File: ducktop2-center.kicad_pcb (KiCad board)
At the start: 8 copper layers, 230 x 185 mm, 710 parts, among them J10 Amphenol MDT420M01001 M-key N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, J16 Case power/reset button harne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, J2300 FH12-30S 30-pin radio daughte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, J310 Mainboard keyboard FFC to MX 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, J4 TC2030 Cortex SWD: VTref/SWDI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, J40 Amphenol MDT420E01001 E-key W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, J41 SSD1306 OLED A 4-pin GND/VDD/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, J420 Left 8-ohm BTL speaker; pin 1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, J421 Right 8-ohm BTL speaker; pin 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, J422 CUI SJ1-3535NG rear 3.5mm ste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, J45 SSD1306 OLED B 4-pin GND/VDD/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, J52 Delta BFB04512HHA-CZ0T: GND, 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, J53 Lid/hall switch, J54 Skin/hinge NTC, J56 Mu heatsink/spreader NTC, J58 Field-soldered trackpad USB2 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, J73 Rear USB-C EC firmware progra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, J901 JST PUD 2x20 protected maker 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, J902 TC2030 Cortex SWD: VTref/SWDI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, Q13 CSD19537Q3 100V AUX reverse F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, Q14 BSS138 fast reverse-gate pull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, Q200 2N7002KT1G fan PWM open-drain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, Q21 SiSS4409DN 40V reverse-blocki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, Q22 SiSS4409DN 40V reverse-blocki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, Q23 SiSS4409DN 40V reverse-blocki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, Q2300 2N7002K radio-PG USB enable, Q24 SiSS4409DN 40V reverse-blocki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, Q25 CSD17575Q3 BQ25798 ship FET, Q60 2N7002 physical host-VBUS USB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, Q62 2N7002 DFU-mode USB mux force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, Q700 BSS138 active-high charger en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, Q702 BSS138 QON open-drain pulse, Q750 BSS138 fail-off EN/UVLO clamp, Q751 BSS138 active-high enable rel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, Q901 2N7002 physical host-VBUS USB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, Q903 2N7002 maker header isolation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, SW1 Reset, SW2 Mu Power, SW3 Mu Reset, SW4 BOOT0 (DFU), SW900 Maker reset/RUN, SW901 Maker BOOTSEL, U10 BQ34Z100-G1 protected-pack ga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, U12 TPS26630RGER 3A AUX eFuse / s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, U15 LTC4418IUF#PBF dual-input sel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, U170 SN74LVC3G34DCUR E-key control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, U2 BQ25798RQMR, U2300 TPS259470ARPW 2A reverse-bloc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, U2301 TLV803EA43 4.3V radio rail su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, U2302 SN74LVC1G17DBVR radio PG leve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, U2303 TS3USB30E default-disconnecte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, U2304 TPS2553D radio codec VBUS gat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, U2305 USBLC6-2P6 radio codec USB ESD, U310 TPS2553D keyboard RGB 5V swit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, U311 SN74AHCT1G126 keyboard RGB 3V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, U4 STM32F407VGTx, U400 USB2512B-AEZG-TR two-port HS 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, U401 TLV803EA29RDBZR 2.93V reset s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, U402 TPS2052BDR dual 500mA USB pow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, U410 PCM2900CDBR USB Audio Class s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, U420 TPA2012D2RTJR stereo BTL clas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, U421 SN74LVC1G08DBVR SSPND AND EC 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, U425 TPA6130A2RTJR DirectPath ster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, U430 LP5907MFX-2.8/NOPB low-noise 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, U431 TLV9061IDBVR microphone pream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, U44 TCA9539PWR resettable source 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, U45 TCA9548A service I2C mux @0x70, U46 SN74LVC1G08DBVR EC-reset-qual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, U5 TPS54202DDC, U6 TPS56637RPAR VSYS -> SYS_5V (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, U60 USBLC6-2P6 EC USB ESD, U61 TS3USB30EDGSR EC USB host-sta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, U62 TPD4E05U06 wired trackpad USB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, U63 USBLC6-2P6 EC DFU USB ESD, U64 TPS2553DDBVR trackpad 0.61A b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, U7 TPS56637RPAR VSYS -> SYS_3V3 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, U718 TPS259470ARPW aggregate EC AO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, U750 TPS552892RYQR 12V buck-boost, U769 SN74LVC1G08DBVR qualified hos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, U770 TPS2553DDBVR internal host VB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

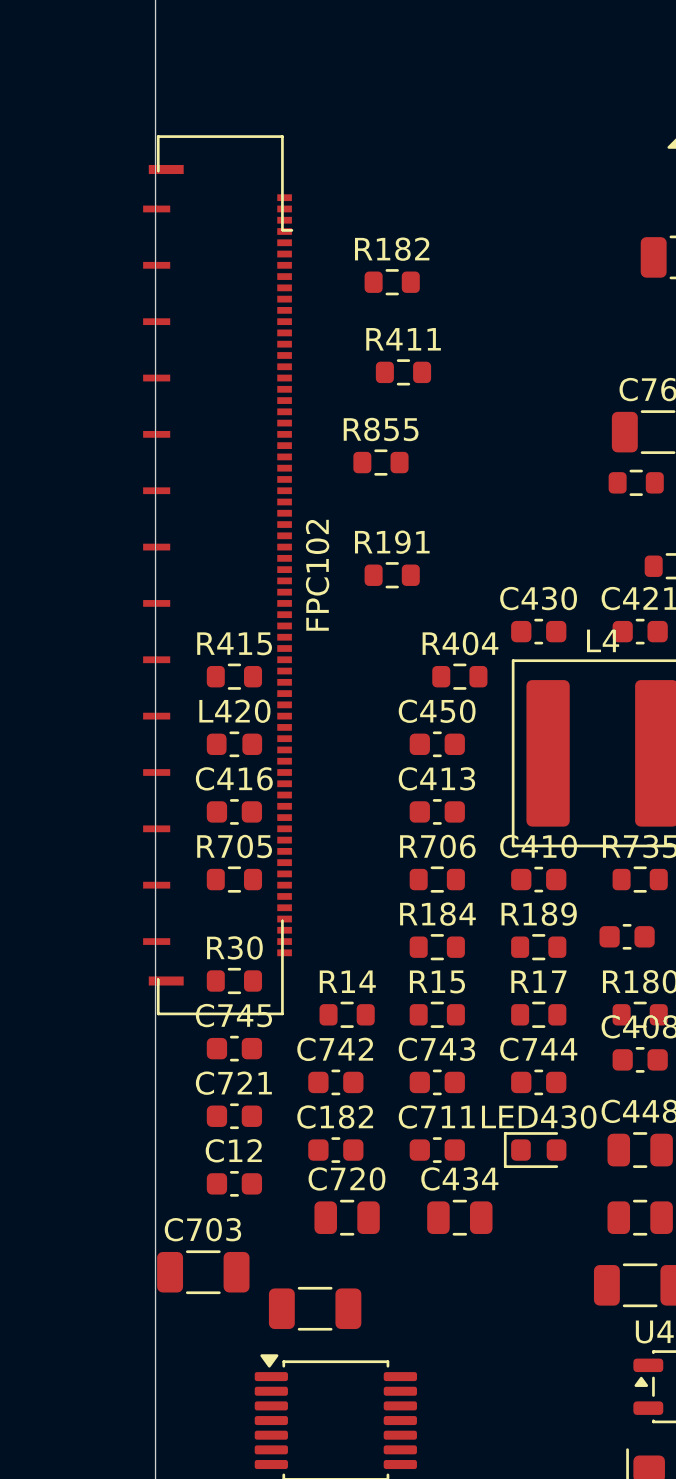
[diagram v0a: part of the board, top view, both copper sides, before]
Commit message: Deep audit completion: FPC anchors over cut lines, FPC106 rotation, pro rules
Follow-up fixes found while closing out the audit:
- FPC102/FPC104 FH41 MP tabs poked across the internal cut lines (pads
  physically off their boards): anchors moved to (73.5, 92.5) and
  (303.6, 92.5); all four boards now report 0 boundary crossings.
- FPC106 had reverted to the seam-away rotation; restored to (30, 54)
  rot 0 (cable enters from the BMS top edge).
- The MCP board sync clobbers the daughterboard .kicad_pro design rules;
  inherit_netclasses now restores them (min_through_hole 0.2, min_track
  0.09, min_clearance 0.09) so the DRC is honest about the 0.2mm drills.
- ERC triaged on all four projects: remaining items are cross-board
  power nets (driver on the other side of an FPC), power-flag artifacts,
  or intentional NCs -- no genuine errors.
- FH41-68S-0.5SH confirmed orderable (DigiKey/Mouser in stock).
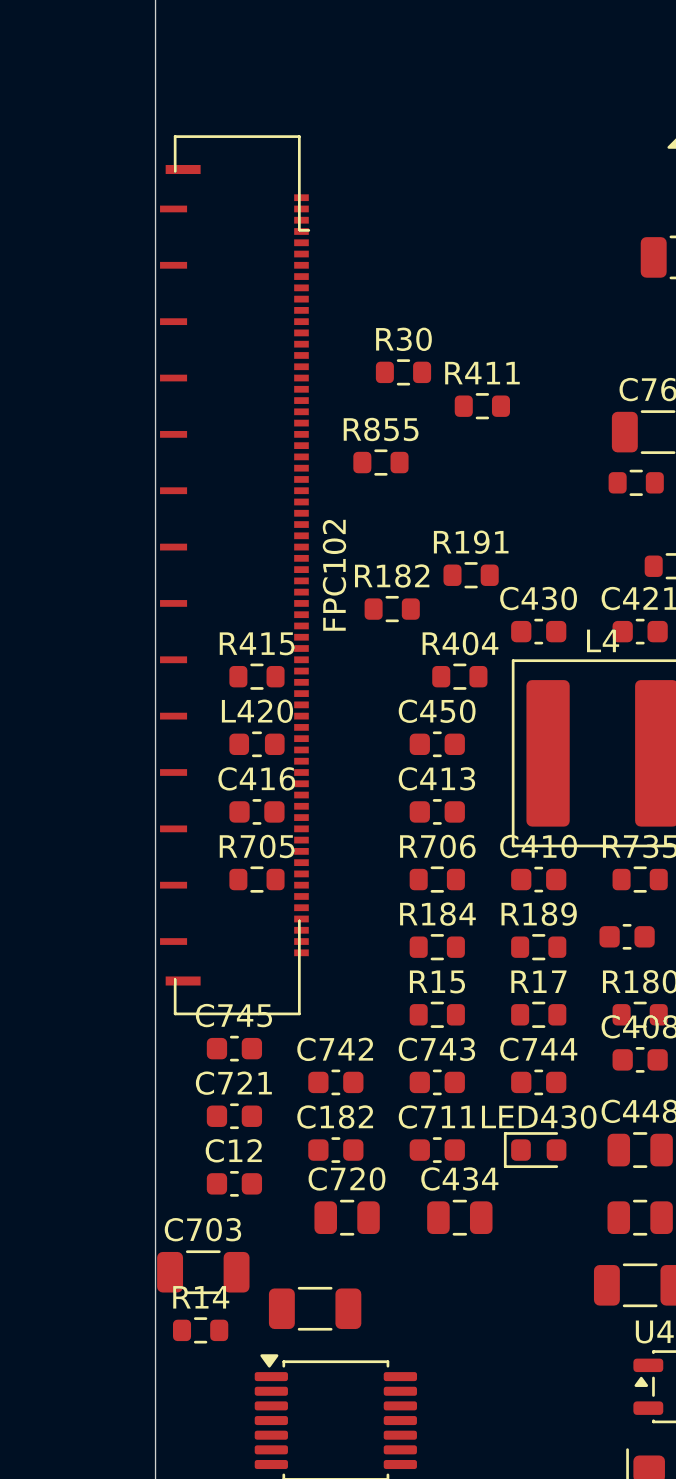
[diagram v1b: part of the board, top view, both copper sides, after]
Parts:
- moved R30 28.0 mm to (81.0, 83.5)
- moved R14 15.4 mm to (72.0, 126.0)
- moved R182 14.5 mm to (80.5, 94.0)
- moved R411 3.81 mm to (84.5, 85.0)
- moved R191 3.50 mm to (84.0, 92.5)
- moved C416 1.00 mm to (74.5, 103.0)
- moved L420 1.00 mm to (74.5, 100.0)
- moved R415 1.00 mm to (74.5, 97.0)
- moved R705 1.00 mm to (74.5, 106.0)
- moved FPC102 0.75 mm to (73.5, 92.5)

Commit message: Phase 5: second-opinion audit remediation + rebuilt, verified board pipeline
Second-opinion AI audit found A-tier defects; remediation applied and the
board pipeline rebuilt on a known-good base with the fixes it needed:

- electrical: LTC4418IUF symbol pinout corrected (both selectors were
  dead as drawn); center charge cascade (U15 <- U15B, PD1 > PD2 > AUX);
  pack negative never crosses FPC-3, 15-pin FG_VSS return; power-budgeted
  FPC pin maps (0.4 A/pin derate); J12/DS4 completed; AUX source fuse
- FH41-68S footprint: 13 datasheet-correct SH pads + SH pin in symbol
- connector geometry settled against the Hirose FH12 2D drawing: FFC
  enters opposite the solder pins (mouth = local +Y); reversed side-B
  maps are correct for the 180-deg-mounted pairs; rotations set so mouths
  face across every seam
- pipeline (generate_split_boards.py): per-pin pad-net resync from the
  netlists (kills shadow nets for good), netlist-exact name
  normalization, netlist-only part injection (cascade, probe headers),
  zone refill after outline swap, read-before-write race fixed, orphan
  parts dropped loudly, non-zero exit on unresolved overlaps
- monolith board relocated to old/monolith_ducktop2.kicad_pcb (placement
  oracle for the center cut only)

verified end state: 4 boards 0 shorts / 0 clearance / 0 drill, 0 boundary
crossings, 6/6 connectors contract-exact with mouths facing, 0 shadow
nets, gates PASS x4, ERC 0 x4. routing next (499 nets/board).
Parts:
- added C715: C_0402_1005Metric, C_0402_1005Metric, F.Cu at (141.0, 7.00)
- added C747: C_0603_1608Metric, C_0603_1608Metric, F.Cu at (141.0, 8.50)
- added C748: C_0603_1608Metric, C_0603_1608Metric, F.Cu at (141.0, 15.5)
- added C749: C_0603_1608Metric, C_0603_1608Metric, F.Cu at (141.0, 22.0)
- added J50: PinHeader_1x04_P2.54mm_Vertical, PinHeader_1x04_P2.54mm_Vertical, F.Cu at (141.0, 44.5)
- added J8: PinHeader_1x04_P2.54mm_Vertical, PinHeader_1x04_P2.54mm_Vertical, F.Cu at (186.0, 90.0)
- added Q26: Vishay_PowerPAK_1212-8_Single, Vishay_PowerPAK_1212-8_Single, F.Cu at (186.0, 102.0)
- added Q27: Vishay_PowerPAK_1212-8_Single, Vishay_PowerPAK_1212-8_Single, F.Cu at (186.0, 114.0)
- added Q28: Vishay_PowerPAK_1212-8_Single, Vishay_PowerPAK_1212-8_Single, F.Cu at (195.0, 30.0)
- added Q29: Vishay_PowerPAK_1212-8_Single, Vishay_PowerPAK_1212-8_Single, F.Cu at (195.0, 42.0)
- added R741: R_0603_1608Metric, R_0603_1608Metric, F.Cu at (195.0, 54.0)
- added R742: R_0603_1608Metric, R_0603_1608Metric, F.Cu at (195.0, 66.0)
- added R743: R_0603_1608Metric, R_0603_1608Metric, F.Cu at (195.0, 78.0)
- added R744: R_0603_1608Metric, R_0603_1608Metric, F.Cu at (150.0, 45.0)
- added R745: R_0603_1608Metric, R_0603_1608Metric, F.Cu at (150.0, 57.0)
- added R746: R_0603_1608Metric, R_0603_1608Metric, F.Cu at (150.0, 69.0)
- added R747: R_0603_1608Metric, R_0603_1608Metric, F.Cu at (159.0, 1.50)
- added U15B: ADI_UF20_QFN20_4x4_P0.5_EP2.45, ADI_UF20_QFN20_4x4_P0.5_EP2.45, F.Cu at (204.0, 42.0)
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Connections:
- net /EC & MCU/BOOT0_NET renamed /EC &amp; MCU/BOOT0_NET
- net /EC & MCU/BUCK_BOOT renamed /EC &amp; MCU/BUCK_BOOT
- net /EC & MCU/BUCK_FB renamed /EC &amp; MCU/BUCK_FB
- net /EC & MCU/BUCK_SW renamed /EC &amp; MCU/BUCK_SW
- net /EC & MCU/EC_SWD_VTREF renamed /EC &amp; MCU/EC_SWD_VTREF
- net /EC & MCU/HSE_IN renamed /EC &amp; MCU/HSE_IN
- net /EC & MCU/HSE_OUT renamed /EC &amp; MCU/HSE_OUT
- net /EC & MCU/HSE_XTAL_OUT renamed /EC &amp; MCU/HSE_XTAL_OUT
- net /EC & MCU/LSE_IN renamed /EC &amp; MCU/LSE_IN
- net /EC & MCU/LSE_OUT renamed /EC &amp; MCU/LSE_OUT
- net /EC & MCU/NRST_NET renamed /EC &amp; MCU/NRST_NET
- net /EC & MCU/SERVICE_MUX_RESET_REQ_N renamed /EC &amp; MCU/SERVICE_MUX_RESET_REQ_N
- net /EC & MCU/SOURCE_MGR_INT_N renamed /EC &amp; MCU/SOURCE_MGR_INT_N
- net /EC & MCU/SWCLK_NET renamed /EC &amp; MCU/SWCLK_NET
- net /EC & MCU/SWDIO_NET renamed /EC &amp; MCU/SWDIO_NET
- net /EC & MCU/VCAP1_NODE renamed /EC &amp; MCU/VCAP1_NODE
- net /EC & MCU/VCAP2_NODE renamed /EC &amp; MCU/VCAP2_NODE
- net /Power & Battery/AON_EFUSE_DVDT renamed /Power &amp; Battery/AON_EFUSE_DVDT
- net /Power & Battery/AON_EFUSE_ILM renamed /Power &amp; Battery/AON_EFUSE_ILM
- net /Power & Battery/AON_EFUSE_OV renamed /Power &amp; Battery/AON_EFUSE_OV
- net /Power & Battery/AON_EFUSE_UV renamed /Power &amp; Battery/AON_EFUSE_UV
- net /Power & Battery/AON_OR_RAW renamed /Power &amp; Battery/AON_OR_RAW
- net /Power & Battery/AUX_DC_DIV renamed /Power &amp; Battery/AUX_DC_DIV
- net /Power & Battery/AUX_DC_FUSED renamed /Power &amp; Battery/AUX_DC_FUSED
- net /Power & Battery/AUX_EFUSE_BGATE renamed /Power &amp; Battery/AUX_EFUSE_BGATE
- net /Power & Battery/AUX_EFUSE_DRV renamed /Power &amp; Battery/AUX_EFUSE_DRV
- net /Power & Battery/AUX_EFUSE_DVDT renamed /Power &amp; Battery/AUX_EFUSE_DVDT
- net /Power & Battery/AUX_EFUSE_ILIM renamed /Power &amp; Battery/AUX_EFUSE_ILIM
- net /Power & Battery/AUX_EFUSE_IN_SYS renamed /Power &amp; Battery/AUX_EFUSE_IN_SYS
- net /Power & Battery/AUX_EFUSE_OV renamed /Power &amp; Battery/AUX_EFUSE_OV
- net /Power & Battery/AUX_EFUSE_Q2_GATE renamed /Power &amp; Battery/AUX_EFUSE_Q2_GATE
- net /Power & Battery/AUX_EFUSE_UV renamed /Power &amp; Battery/AUX_EFUSE_UV
- net /Power & Battery/AUX_PGTH renamed /Power &amp; Battery/AUX_PGTH
- net /Power & Battery/BATP_SENSE renamed /Power &amp; Battery/BATP_SENSE
- net /Power & Battery/BAT_CHARGER renamed /Power &amp; Battery/BAT_CHARGER
- net /Power & Battery/BTST1_NODE renamed /Power &amp; Battery/BTST1_NODE
- net /Power & Battery/BTST2_NODE renamed /Power &amp; Battery/BTST2_NODE
- net /Power & Battery/CHG_CE_HW_N renamed /Power &amp; Battery/CHG_CE_HW_N
- net /Power & Battery/CHG_TS_FIXED renamed /Power &amp; Battery/CHG_TS_FIXED
- net /Power & Battery/FG_BAT_DIV renamed /Power &amp; Battery/FG_BAT_DIV
- net /Power & Battery/FG_BAT_SENSE renamed /Power &amp; Battery/FG_BAT_SENSE
- net /Power & Battery/FG_CE renamed /Power &amp; Battery/FG_CE
- net /Power & Battery/FG_P1_TIE renamed /Power &amp; Battery/FG_P1_TIE
- net /Power & Battery/FG_REG25 renamed /Power &amp; Battery/FG_REG25
- net /Power & Battery/FG_SRN renamed /Power &amp; Battery/FG_SRN
- net /Power & Battery/FG_SRP renamed /Power &amp; Battery/FG_SRP
- net /Power & Battery/FG_TS renamed /Power &amp; Battery/FG_TS
- net /Power & Battery/ILIM_SET renamed /Power &amp; Battery/ILIM_SET
- net /Power & Battery/MAIN_SEL_TMR renamed /Power &amp; Battery/MAIN_SEL_TMR
- net /Power & Battery/PMIC_QON_PIN renamed /Power &amp; Battery/PMIC_QON_PIN
- net /Power & Battery/PMID renamed /Power &amp; Battery/PMID
- net /Power & Battery/PROG_SET renamed /Power &amp; Battery/PROG_SET
- net /Power & Battery/REGN renamed /Power &amp; Battery/REGN
- net /Power & Battery/SDRV_GATE renamed /Power &amp; Battery/SDRV_GATE
- net /Power & Battery/STAT_DRV renamed /Power &amp; Battery/STAT_DRV
- net /Power & Battery/STAT_LED_A renamed /Power &amp; Battery/STAT_LED_A
- net /Power & Battery/SW1 renamed /Power &amp; Battery/SW1
- net /Power & Battery/SW2 renamed /Power &amp; Battery/SW2
- net /Power & Battery/USB_MAIN_FET_COMMON renamed /Power &amp; Battery/USB_MAIN_FET_COMMON
- net /Power & Battery/USB_MAIN_GATE renamed /Power &amp; Battery/USB_MAIN_GATE
- net /Power & Battery/USB_MAIN_OV renamed /Power &amp; Battery/USB_MAIN_OV
- net /Power & Battery/USB_MAIN_UV renamed /Power &amp; Battery/USB_MAIN_UV
- net /Power & Battery/VBUS_DAMP renamed /Power &amp; Battery/VBUS_DAMP
- net /Wi-Fi/Bluetooth & OLEDs/OLED_A_SCL renamed /Wi-Fi/Bluetooth &amp; OLEDs/OLED_A_SCL
- net /Wi-Fi/Bluetooth & OLEDs/OLED_A_SDA renamed /Wi-Fi/Bluetooth &amp; OLEDs/OLED_A_SDA
- net /Wi-Fi/Bluetooth & OLEDs/OLED_B_SCL renamed /Wi-Fi/Bluetooth &amp; OLEDs/OLED_B_SCL
- net /Wi-Fi/Bluetooth & OLEDs/OLED_B_SDA renamed /Wi-Fi/Bluetooth &amp; OLEDs/OLED_B_SDA
- net /Wi-Fi/Bluetooth & OLEDs/WIFI_3V3 renamed /Wi-Fi/Bluetooth &amp; OLEDs/WIFI_3V3
- net /Wi-Fi/Bluetooth & OLEDs/WIFI_PERST_N renamed /Wi-Fi/Bluetooth &amp; OLEDs/WIFI_PERST_N
- net /Wi-Fi/Bluetooth & OLEDs/WIFI_REFCLK_E_N renamed /Wi-Fi/Bluetooth &amp; OLEDs/WIFI_REFCLK_E_N
- net /Wi-Fi/Bluetooth & OLEDs/WIFI_REFCLK_E_P renamed /Wi-Fi/Bluetooth &amp; OLEDs/WIFI_REFCLK_E_P
- net /Wi-Fi/Bluetooth & OLEDs/WIFI_W_DISABLE1_N renamed /Wi-Fi/Bluetooth &amp; OLEDs/WIFI_W_DISABLE1_N
- net /Wi-Fi/Bluetooth & OLEDs/WIFI_W_DISABLE2_N renamed /Wi-Fi/Bluetooth &amp; OLEDs/WIFI_W_DISABLE2_N
- A1 pad 104: (no net) -> unconnected-(A1-~{SMB_ALERT}-Pad104)
- A1 pad 106: (no net) -> unconnected-(A1-SMB_CLK-Pad106)
- A1 pad 108: (no net) -> unconnected-(A1-SMB_DATA-Pad108)
- A1 pad 112: (no net) -> unconnected-(A1-USB2_P6+-Pad112)
- A1 pad 114: (no net) -> unconnected-(A1-USB2_P6--Pad114)
- A1 pad 117: (no net) -> unconnected-(A1-~{PROCHOT}-Pad117)
- A1 pad 118: (no net) -> unconnected-(A1-GPP_F16-Pad118)
- A1 pad 119: (no net) -> unconnected-(A1-GPP_E0-Pad119)
- A1 pad 120: (no net) -> unconnected-(A1-GPP_F15-Pad120)
- A1 pad 121: (no net) -> unconnected-(A1-GPP_A12-Pad121)
- A1 pad 122: (no net) -> unconnected-(A1-GPP_F14-Pad122)
- A1 pad 123: (no net) -> unconnected-(A1-GPP_B14-Pad123)
- A1 pad 124: (no net) -> unconnected-(A1-GPP_F13-Pad124)
- A1 pad 125: (no net) -> unconnected-(A1-GPP_B11-Pad125)
- A1 pad 126: (no net) -> unconnected-(A1-GPP_F12-Pad126)
- A1 pad 127: (no net) -> unconnected-(A1-TPM_IRQ-Pad127)
- A1 pad 128: (no net) -> unconnected-(A1-GPP_D0-Pad128)
- A1 pad 130: (no net) -> unconnected-(A1-GPP_D1-Pad130)
- A1 pad 131: (no net) -> unconnected-(A1-SUSCLK-Pad131)
- A1 pad 132: (no net) -> unconnected-(A1-GPP_D2-Pad132)
- A1 pad 133: (no net) -> unconnected-(A1-~{BIOS_SEL}-Pad133)
- A1 pad 134: (no net) -> unconnected-(A1-GPP_D3-Pad134)
- A1 pad 137: (no net) -> unconnected-(A1-UART0_RXD-Pad137)
- A1 pad 138: (no net) -> unconnected-(A1-UART2_TXD-Pad138)
- A1 pad 139: (no net) -> unconnected-(A1-UART0_TXD-Pad139)
- A1 pad 140: (no net) -> unconnected-(A1-UART2_RXD-Pad140)
- A1 pad 141: (no net) -> unconnected-(A1-UART1_RXD-Pad141)
- A1 pad 142: (no net) -> unconnected-(A1-I2C5_SCL-Pad142)
- A1 pad 143: (no net) -> unconnected-(A1-UART1_TXD-Pad143)
- A1 pad 144: (no net) -> unconnected-(A1-I2C5_SDA-Pad144)
- A1 pad 145: (no net) -> unconnected-(A1-SML1_DATA-Pad145)
- A1 pad 146: (no net) -> unconnected-(A1-I2C4_SCL-Pad146)
- A1 pad 147: (no net) -> unconnected-(A1-SML1_CLK-Pad147)
- A1 pad 148: (no net) -> unconnected-(A1-I2C4_SDA-Pad148)
- A1 pad 149: (no net) -> unconnected-(A1-~{SML1_ALERT}-Pad149)
- A1 pad 150: (no net) -> unconnected-(A1-I2C3_SCL-Pad150)
- A1 pad 152: (no net) -> unconnected-(A1-I2C3_SDA-Pad152)
- A1 pad 153: (no net) -> unconnected-(A1-SPI_IO3-Pad153)
- A1 pad 154: (no net) -> unconnected-(A1-I2C2_SCL-Pad154)
- A1 pad 155: (no net) -> unconnected-(A1-SPI_CLK-Pad155)
- A1 pad 156: (no net) -> unconnected-(A1-I2C2_SDA-Pad156)
- A1 pad 157: (no net) -> unconnected-(A1-~{SPI_CS2}-Pad157)
- A1 pad 159: (no net) -> unconnected-(A1-SPI_MOSI/SPI_IO0-Pad159)
- A1 pad 160: (no net) -> unconnected-(A1-I2S_MCLK-Pad160)
- A1 pad 161: (no net) -> unconnected-(A1-SPI_IO2-Pad161)
- A1 pad 162: (no net) -> unconnected-(A1-I2S_SCLK-Pad162)
- A1 pad 163: (no net) -> unconnected-(A1-SPI_MISO/SPI_IO1-Pad163)
- A1 pad 164: (no net) -> unconnected-(A1-I2S_SFRM-Pad164)
- A1 pad 165: (no net) -> unconnected-(A1-~{SPI_CS}-Pad165)
- A1 pad 166: (no net) -> unconnected-(A1-I2S_TXD-Pad166)
- A1 pad 168: (no net) -> unconnected-(A1-I2S_RXD-Pad168)
- A1 pad 169: (no net) -> unconnected-(A1-DDIB_DDC_SDA-Pad169)
- A1 pad 171: (no net) -> unconnected-(A1-DDIB_DDC_SCL-Pad171)
- A1 pad 172: (no net) -> unconnected-(A1-HDA_RST-Pad172)
- A1 pad 173: (no net) -> unconnected-(A1-TCP1_DDC_SDA-Pad173)
- A1 pad 174: (no net) -> unconnected-(A1-HDA_BCLK-Pad174)
- A1 pad 175: (no net) -> unconnected-(A1-TCP1_DDC_SCL-Pad175)
- A1 pad 176: (no net) -> unconnected-(A1-HDA_SYNC-Pad176)
- A1 pad 178: (no net) -> unconnected-(A1-HDA_SDOUT-Pad178)
- A1 pad 180: (no net) -> unconnected-(A1-HDA_SDIN-Pad180)
- A1 pad 183: (no net) -> unconnected-(A1-DDIB_HPD-Pad183)
- A1 pad 184: (no net) -> unconnected-(A1-CSI_D_CK+-Pad184)
- A1 pad 185: (no net) -> unconnected-(A1-TCP1_HPD-Pad185)
- A1 pad 186: (no net) -> unconnected-(A1-CSI_D_CK--Pad186)
- A1 pad 190: (no net) -> unconnected-(A1-CSI_D_D1+/CSI_C_D2+-Pad190)
- A1 pad 191: (no net) -> unconnected-(A1-DDIB_AUX--Pad191)
- A1 pad 192: (no net) -> unconnected-(A1-CSI_D_D1-/CSI_C_D2--Pad192)
- A1 pad 193: (no net) -> unconnected-(A1-DDIB_AUX+-Pad193)
- A1 pad 196: (no net) -> unconnected-(A1-CSI_D_D0+/CSI_C_D3+-Pad196)
- A1 pad 197: (no net) -> unconnected-(A1-DDIB_TX3--Pad197)
- A1 pad 198: (no net) -> unconnected-(A1-CSI_D_D0-/CSI_C_D3--Pad198)
- A1 pad 199: (no net) -> unconnected-(A1-DDIB_TX3+-Pad199)
- A1 pad 2: (no net) -> unconnected-(A1-FAN1_PWM-Pad2)
- A1 pad 202: (no net) -> unconnected-(A1-CSI_C_CK+-Pad202)
- A1 pad 203: (no net) -> unconnected-(A1-DDIB_TX2--Pad203)
- A1 pad 204: (no net) -> unconnected-(A1-CSI_C_CK--Pad204)
- A1 pad 205: (no net) -> unconnected-(A1-DDIB_TX2+-Pad205)
- A1 pad 208: (no net) -> unconnected-(A1-CSI_C_D1+-Pad208)
- A1 pad 209: (no net) -> unconnected-(A1-DDIB_TX1--Pad209)
- A1 pad 210: (no net) -> unconnected-(A1-CSI_C_D1--Pad210)
- A1 pad 211: (no net) -> unconnected-(A1-DDIB_TX1+-Pad211)
- A1 pad 214: (no net) -> unconnected-(A1-CSI_C_D0+-Pad214)
- A1 pad 215: (no net) -> unconnected-(A1-DDIB_TX0--Pad215)
- A1 pad 216: (no net) -> unconnected-(A1-CSI_C_D0--Pad216)
- A1 pad 217: (no net) -> unconnected-(A1-DDIB_TX0+-Pad217)
- A1 pad 220: (no net) -> unconnected-(A1-TCP1_TX0+-Pad220)
- A1 pad 221: (no net) -> unconnected-(A1-TCP0_AUX--Pad221)
- A1 pad 222: (no net) -> unconnected-(A1-TCP1_TX0--Pad222)
- A1 pad 223: (no net) -> unconnected-(A1-TCP0_AUX+-Pad223)
- A1 pad 226: (no net) -> unconnected-(A1-TCP1_TXRX0+-Pad226)
- A1 pad 228: (no net) -> unconnected-(A1-TCP1_TXRX0--Pad228)
- A1 pad 232: (no net) -> unconnected-(A1-TCP1_TX1+-Pad232)
- A1 pad 234: (no net) -> unconnected-(A1-TCP1_TX1--Pad234)
- A1 pad 238: (no net) -> unconnected-(A1-TCP1_TXRX1+-Pad238)
- A1 pad 240: (no net) -> unconnected-(A1-TCP1_TXRX1--Pad240)
- A1 pad 244: (no net) -> unconnected-(A1-TCP1_AUX+-Pad244)
- A1 pad 246: (no net) -> unconnected-(A1-TCP1_AUX--Pad246)
- A1 pad 25: (no net) -> unconnected-(A1-HSIO2_TX+-Pad25)
- A1 pad 27: (no net) -> unconnected-(A1-HSIO2_TX--Pad27)
- A1 pad 28: (no net) -> unconnected-(A1-HSIO2_RX+-Pad28)
- A1 pad 30: (no net) -> unconnected-(A1-HSIO2_RX--Pad30)
- A1 pad 6: (no net) -> unconnected-(A1-FAN2_PWM-Pad6)
- A1 pad 8: (no net) -> unconnected-(A1-FAN2_TAC-Pad8)
- A1 pad 85: (no net) -> unconnected-(A1-REFCLK0+-Pad85)
- A1 pad 87: (no net) -> unconnected-(A1-REFCLK0--Pad87)
- A1 pad 9: (no net) -> unconnected-(A1-TSENSE-Pad9)
- A1 pad 91: (no net) -> unconnected-(A1-REFCLK1+-Pad91)
- A1 pad 93: (no net) -> unconnected-(A1-REFCLK1--Pad93)
- C12 pad 1: /Power & Battery/VBUS_COMBINED -> /Power &amp; Battery/VBUS_COMBINED
- C180 pad 2: /Power & Battery/FG_VSS -> /FG_VSS
- C182 pad 2: /Power & Battery/FG_VSS -> /FG_VSS
- C183 pad 2: /Power & Battery/FG_VSS -> /FG_VSS
- C701 pad 1: /Power & Battery/VBUS_COMBINED -> /Power &amp; Battery/VBUS_COMBINED
- C702 pad 1: /Power & Battery/VBUS_COMBINED -> /Power &amp; Battery/VBUS_COMBINED
- C722 pad 1: /Power & Battery/AUX_DC_PROTECTED -> /Power &amp; Battery/AUX_DC_PROTECTED
- C740 pad 1: /Power & Battery/MAIN_SEL_INTVCC -> /Power &amp; Battery/MAIN_SEL_INTVCC
- C744 pad 1: /Power & Battery/AUX_DC_PROTECTED -> /Power &amp; Battery/AUX_DC_PROTECTED
- C745 pad 1: /Power & Battery/AUX_MAIN_FET_COMMON -> /Power &amp; Battery/ST2_AUX_FET_COMMON
- C746 pad 1: /Power & Battery/VBUS_COMBINED -> /Power &amp; Battery/VBUS_COMBINED
- D711 pad 2: /Power & Battery/AUX_DC_PROTECTED -> /Power &amp; Battery/AUX_DC_PROTECTED
- F190 pad 1: /Power & Battery/AUX_DC_RAW -> /AUX_DC_RAW
- FPC102 pad 1: VSYS -> GND
- FPC102 pad 10: GND -> /USBC1_SSRX_N
- FPC102 pad 11: PD1_VBUS_RAW -> /USBC1_SSRX_P
- FPC102 pad 13: AUX_DC_RAW -> /HUB_DS1_DM
- FPC102 pad 14: GND -> /HUB_DS1_DP
- FPC102 pad 15: USB_PD_SELECTED -> GND
- FPC102 pad 16: GND -> /USBC2_DM
- FPC102 pad 17: INTERNAL_USB_VBUS_VALID -> /USBC2_DP
- FPC102 pad 19: PD1_I2C_SCL -> /USBC1_DM
- FPC102 pad 2: VSYS -> /USBC2_SSTX_N
- FPC102 pad 20: PD1_I2C_SDA -> /USBC1_DP
- FPC102 pad 21: GND -> /HUB_PRT_CTL4
- FPC102 pad 22: PD1_TCPC_IRQ_N -> /HUB_DS4_DM
- FPC102 pad 23: GND -> /HUB_DS4_DP
- FPC102 pad 24: PD1_PATH_EN -> /PD_PROTECT_FAULT_N
- FPC102 pad 25: GND -> /PD1_EFUSE_FAULT_N
- FPC102 pad 26: PD1_VALID_N -> /PD1_VALID_N
- FPC102 pad 27: GND -> /PD1_PATH_EN
- FPC102 pad 28: PD2_VALID_N -> /PD1_TCPC_IRQ_N
- FPC102 pad 29: GND -> /PD1_I2C_SDA
- FPC102 pad 3: GND -> /USBC2_SSTX_P
- FPC102 pad 30: PD1_EFUSE_FAULT_N -> /PD1_I2C_SCL
- FPC102 pad 31: GND -> /INTERNAL_USB_VBUS_VALID
- FPC102 pad 32: PD_PROTECT_FAULT_N -> GND
- FPC102 pad 34: USBC1_DP -> GND
- FPC102 pad 35: USBC1_DM -> /AUX_DC_RAW
- FPC102 pad 36: GND -> /AUX_DC_RAW
- FPC102 pad 37: USBC2_DP -> /AUX_DC_RAW
- FPC102 pad 38: USBC2_DM -> /AUX_DC_RAW
- FPC102 pad 39: GND -> /AUX_DC_RAW
- FPC102 pad 4: USB_PORT_5V -> /USBC2_SSRX_N
- FPC102 pad 40: HUB_DS1_DP -> /AUX_DC_RAW
- FPC102 pad 41: HUB_DS1_DM -> /USB_PD_SELECTED
- FPC102 pad 42: GND -> /USB_PD_SELECTED
- FPC102 pad 43: USBC1_SSRX_P -> /USB_PD_SELECTED
- FPC102 pad 44: USBC1_SSRX_N -> /USB_PD_SELECTED
- FPC102 pad 45: GND -> /USB_PD_SELECTED
- FPC102 pad 46: USBC1_SSTX_P -> /USB_PD_SELECTED
- FPC102 pad 47: USBC1_SSTX_N -> /PD1_VBUS_RAW
- FPC102 pad 48: GND -> /PD1_VBUS_RAW
- FPC102 pad 49: USBC2_SSRX_P -> /PD1_VBUS_RAW
- FPC102 pad 5: USB_PORT_5V -> /USBC2_SSRX_P
- FPC102 pad 50: USBC2_SSRX_N -> /PD1_VBUS_RAW
- FPC102 pad 51: GND -> /PD1_VBUS_RAW
- FPC102 pad 52: USBC2_SSTX_P -> /PD1_VBUS_RAW
- FPC102 pad 53: USBC2_SSTX_N -> /MCU_3V3
- FPC102 pad 54: GND -> /SYS_3V3
- FPC102 pad 55: GND -> /SYS_3V3
- FPC102 pad 57: GND -> /USB_PORT_5V
- FPC102 pad 58: GND -> /USB_PORT_5V
- FPC102 pad 59: GND -> /USB_PORT_5V
- FPC102 pad 60: GND -> /USB_PORT_5V
- FPC102 pad 63: GND -> /VSYS
- FPC102 pad 64: GND -> /VSYS
- FPC102 pad 65: GND -> /VSYS
- FPC102 pad 66: GND -> /VSYS
- FPC102 pad 67: GND -> /VSYS
- FPC102 pad 68: GND -> /VSYS
- FPC102 pad 7: SYS_3V3 -> /USBC1_SSTX_N
- FPC102 pad 8: GND -> /USBC1_SSTX_P
- FPC102 pad 9: MCU_3V3 -> GND
- FPC103 pad 1: SYS_5V -> /TCP0_TXRX1_N
- FPC103 pad 10: GND -> /TCP0_TX0_P
- FPC103 pad 11: MCU_3V3 -> GND
- FPC103 pad 12: GND -> /GBE_HOST_TX_N
- FPC103 pad 13: PD2_VBUS_RAW -> /GBE_HOST_TX_P
- FPC103 pad 15: MU_HOST_ACTIVE -> /GBE_HOST_RX_N
- FPC103 pad 16: GND -> /GBE_HOST_RX_P
- FPC103 pad 17: PLTRST_SRC_N -> GND
- FPC103 pad 18: GND -> /GBE_REFCLK_N
- FPC103 pad 19: PCIE_WAKE_N -> /GBE_REFCLK_P
- FPC103 pad 2: SYS_5V -> /TCP0_TXRX1_P
- FPC103 pad 21: GBE_CLKREQ_N -> /TCP0_HPD
- FPC103 pad 22: GND -> /TCP0_DDC_SDA
- FPC103 pad 23: PD2_I2C_SCL -> /TCP0_DDC_SCL
- FPC103 pad 24: PD2_I2C_SDA -> GND
- FPC103 pad 25: GND -> /HUB_DS1_DM
- FPC103 pad 26: PD2_TCPC_IRQ_N -> /HUB_DS1_DP
- FPC103 pad 28: PD2_PATH_EN -> /PD_PROTECT_FAULT_N
- FPC103 pad 29: GND -> /PD2_EFUSE_FAULT_N
- FPC103 pad 3: GND -> /TCP0_TXRX0_N
- FPC103 pad 30: PD2_EFUSE_FAULT_N -> /PD2_PATH_EN
- FPC103 pad 31: GND -> /PD2_TCPC_IRQ_N
- FPC103 pad 32: PD_PROTECT_FAULT_N -> /PD2_I2C_SDA
- FPC103 pad 33: GND -> /PD2_I2C_SCL
- FPC103 pad 34: HUB_DS1_DP -> /GBE_CLKREQ_N
- FPC103 pad 35: HUB_DS1_DM -> /PCIE_WAKE_N
- FPC103 pad 36: GND -> /PLTRST_SRC_N
- FPC103 pad 37: TCP0_DDC_SCL -> /MU_HOST_ACTIVE
- FPC103 pad 38: TCP0_DDC_SDA -> /HUB_PRT_CTL4
- FPC103 pad 39: GND -> /HUB_DS4_DM
- FPC103 pad 4: USB_PORT_5V -> /TCP0_TXRX0_P
- FPC103 pad 40: TCP0_HPD -> /HUB_DS4_DP
- FPC103 pad 42: GBE_REFCLK_P -> /MCU_3V3
- FPC103 pad 43: GBE_REFCLK_N -> /MCU_3V3
- FPC103 pad 44: GND -> /PCIE_3V3
- FPC103 pad 45: GBE_HOST_RX_P -> /PCIE_3V3
- FPC103 pad 46: GBE_HOST_RX_N -> /SYS_3V3
- FPC103 pad 47: GND -> /SYS_3V3
- FPC103 pad 48: GBE_HOST_TX_P -> GND
- FPC103 pad 49: GBE_HOST_TX_N -> GND
- FPC103 pad 5: USB_PORT_5V -> GND
- FPC103 pad 50: GND -> /USB_PORT_5V
- FPC103 pad 51: TCP0_TX0_P -> /USB_PORT_5V
- FPC103 pad 52: TCP0_TX0_N -> /USB_PORT_5V
- FPC103 pad 53: GND -> /USB_PORT_5V
- FPC103 pad 54: TCP0_TX1_P -> /PD2_VBUS_RAW
- FPC103 pad 55: TCP0_TX1_N -> /PD2_VBUS_RAW
- FPC103 pad 56: GND -> /PD2_VBUS_GATED
- FPC103 pad 57: TCP0_TXRX0_P -> /PD2_VBUS_GATED
- FPC103 pad 58: TCP0_TXRX0_N -> /PD2_VBUS_GATED
- FPC103 pad 59: GND -> /PD2_VBUS_GATED
- FPC103 pad 6: GND -> /TCP0_TX1_N
- FPC103 pad 60: TCP0_TXRX1_P -> /PD2_VBUS_GATED
- FPC103 pad 61: TCP0_TXRX1_N -> /PD2_VBUS_GATED
- FPC103 pad 62: GND -> /PD2_VBUS_GATED
- FPC103 pad 65: GND -> /SYS_5V
- FPC103 pad 66: GND -> /SYS_5V
- FPC103 pad 67: GND -> /SYS_5V
- FPC103 pad 68: GND -> /SYS_5V
- FPC103 pad 7: SYS_3V3 -> /TCP0_TX1_P
- FPC103 pad 9: PCIE_3V3 -> /TCP0_TX0_N
- FPC105 pad 1: PACK_POS_FUSED -> /FG_VSS
- FPC105 pad 10: GND -> /FG_VSS
- FPC105 pad 11: GND -> /FG_VSS
- FPC105 pad 12: GND -> /FG_VSS
- FPC105 pad 13: GND -> /FG_VSS
- FPC105 pad 14: GND -> /FG_VSS
- FPC105 pad 15: GND -> /FG_VSS
- FPC105 pad 16: GND -> /MCU_3V3
- FPC105 pad 17: GND -> /PACK_RETRY_PULSE
- FPC105 pad 18: GND -> /PACK_FAULT_N
- FPC105 pad 19: GND -> /PACK_POS_FUSED
- FPC105 pad 2: PACK_POS_FUSED -> /FG_VSS
- FPC105 pad 20: GND -> /PACK_POS_FUSED
- FPC105 pad 21: GND -> /PACK_POS_FUSED
- FPC105 pad 22: GND -> /PACK_POS_FUSED
- FPC105 pad 23: GND -> /PACK_POS_FUSED
- FPC105 pad 24: GND -> /PACK_POS_FUSED
- FPC105 pad 25: GND -> /PACK_POS_FUSED
- FPC105 pad 26: GND -> /PACK_POS_FUSED
- FPC105 pad 27: GND -> /PACK_POS_FUSED
- FPC105 pad 28: GND -> /PACK_POS_FUSED
- FPC105 pad 29: GND -> /PACK_POS_FUSED
- FPC105 pad 3: GND -> /FG_VSS
- FPC105 pad 30: GND -> /PACK_POS_FUSED
- FPC105 pad 4: GND -> /FG_VSS
- FPC105 pad 5: PACK_FAULT_N -> /FG_VSS
- FPC105 pad 6: PACK_RETRY_PULSE -> /FG_VSS
- FPC105 pad 7: FG_VSS -> /FG_VSS
- FPC105 pad 8: MCU_3V3 -> /FG_VSS
- FPC105 pad 9: GND -> /FG_VSS
- J10 pad 10: (no net) -> unconnected-(J10-DAS/~{DSS}/~{LED1}-Pad10)
- J10 pad 20: (no net) -> unconnected-(J10-NC-Pad20)
- J10 pad 22: (no net) -> unconnected-(J10-NC-Pad22)
- J10 pad 24: (no net) -> unconnected-(J10-NC-Pad24)
- J10 pad 26: (no net) -> unconnected-(J10-NC-Pad26)
- J10 pad 28: (no net) -> unconnected-(J10-NC-Pad28)
- J10 pad 30: (no net) -> unconnected-(J10-NC-Pad30)
- J10 pad 32: (no net) -> unconnected-(J10-NC-Pad32)
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
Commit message: wire the oleds and clean up the center board
fix the hdmi 5v budget in the schematic and add the routing rules. the right pcb sync and remaining placement work are still next.
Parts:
- removed J50, J8: PinHeader_1x04_P2.54mm_Vertical, PinHeader_1x04_P2.54mm_Vertical
- C715: value C_0402_1005Metric -> 15n 50V stage2 TMR approx 240ms; footprint C_0402_1005Metric -> Capacitor_SMD:C_0402_1005Metric
- C744: value 100n 50V AUX V2 local -> 100n 50V stage2 V2 local
- C747: value C_0603_1608Metric -> 100n 50V stage2 VS1 local; footprint C_0603_1608Metric -> Capacitor_SMD:C_0603_1608Metric
- C748: value C_0603_1608Metric -> 100n 50V stage2 out local; footprint C_0603_1608Metric -> Capacitor_SMD:C_0603_1608Metric
- C749: value C_0603_1608Metric -> 100n 10V stage2 INTVCC; footprint C_0603_1608Metric -> Capacitor_SMD:C_0603_1608Metric
- FPC102: value Hirose_FH41-68S-0.5SH_1x68_1MP_1SH_P0.5mm_Horizontal -> FH41-68S-0.5SH (FPC-1)
- FPC103: value Hirose_FH41-68S-0.5SH_1x68_1MP_1SH_P0.5mm_Horizontal -> FH41-68S-0.5SH (FPC-2)
- FPC105: value Hirose_FH12-30S-0.5SH_1x30-1MP_P0.50mm_Horizontal -> FH12-30S-0.5SH (FPC-3)
- J41: value SSD1306 OLED A 4-pin GND/VDD/SCK/SDA -> OLED A cable: GND/3V3/SCL/SDA; footprint ducktop2:SSD1306_0.96in_Module_4Pin -> Connector_JST:JST_GH_SM04B-GHS-TB_1x04-1MP_P1.25mm_Horizontal
- J45: value SSD1306 OLED B 4-pin GND/VDD/SCK/SDA -> OLED B cable: GND/3V3/SCL/SDA; footprint ducktop2:SSD1306_0.96in_Module_4Pin -> Connector_JST:JST_GH_SM04B-GHS-TB_1x04-1MP_P1.25mm_Horizontal
- Q25: footprint ducktop2:CSD19537Q3_DQG -> ducktop2:CSD17575Q3_DQG
- Q26, Q27, Q28, Q29: value Vishay_PowerPAK_1212-8_Single -> SiSS4409DN 40V reverse-blocking PMOS; footprint Vishay_PowerPAK_1212-8_Single -> Package_SO:Vishay_PowerPAK_1212-8_Single
- R40: value 76.8k 0.1% TPS56637 FB high -> 75.0k 0.1% TPS56637 FB high
- R741: value R_0603_1608Metric -> 1.00M 0.1% PD2 UV top; footprint R_0603_1608Metric -> Resistor_SMD:R_0603_1608Metric
- R742: value R_0603_1608Metric -> 19.6k 0.1% PD2 window middle; footprint R_0603_1608Metric -> Resistor_SMD:R_0603_1608Metric
- R743: value R_0603_1608Metric -> 63.4k 0.1% PD2 OV bottom; footprint R_0603_1608Metric -> Resistor_SMD:R_0603_1608Metric
- R744: value R_0603_1608Metric -> 374k 0.1% stage2 UV top; footprint R_0603_1608Metric -> Resistor_SMD:R_0603_1608Metric
- R745: value R_0603_1608Metric -> 54.9k 0.1% stage2 window middle; footprint R_0603_1608Metric -> Resistor_SMD:R_0603_1608Metric
- R746: value R_0603_1608Metric -> 20.0k 0.1% stage2 OV bottom; footprint R_0603_1608Metric -> Resistor_SMD:R_0603_1608Metric
- R747: value R_0603_1608Metric -> 10k PD2 VALID pull-up; footprint R_0603_1608Metric -> Resistor_SMD:R_0603_1608Metric
- U15: value LTC4418IUF#PBF dual-input selector -> LTC4418IUF#PBF dual-input selector (stage 1)
- U15B: value ADI_UF20_QFN20_4x4_P0.5_EP2.45 -> LTC4418IUF#PBF dual-input selector (stage 2); footprint ADI_UF20_QFN20_4x4_P0.5_EP2.45 -> ducktop2:ADI_UF20_QFN20_4x4_P0.5_EP2.45
- moved J41 59.3 mm to (271.5, 27.5), turned to -90 degrees
- moved J901 45.8 mm to (255.5, 65.0), turned to 90 degrees
- moved U2305 4.78 mm to (157.4, 9.50)
- moved C416 4.70 mm to (79.2, 103.0)
- moved L420 4.70 mm to (79.2, 100.0)
- moved R37 4.70 mm to (293.8, 113.3)
- moved R415 4.70 mm to (79.2, 97.0)
- moved R705 4.70 mm to (79.2, 106.0)
- moved R780 4.63 mm to (289.3, 104.3)
- moved R772 4.50 mm to (125.5, 37.5)
- moved C925 4.34 mm to (297.2, 71.8)
- moved R919 3.83 mm to (267.3, 23.1)
- moved R377 3.70 mm to (78.0, 4.80)
- moved C750 3.50 mm to (121.1, 69.4)
- moved R917 3.42 mm to (270.6, 15.1)
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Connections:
- net /EC &amp; MCU/BOOT0_NET renamed /EC & MCU/BOOT0_NET
- net /EC &amp; MCU/BUCK_BOOT renamed /EC & MCU/BUCK_BOOT
- net /EC &amp; MCU/BUCK_FB renamed /EC & MCU/BUCK_FB
- net /EC &amp; MCU/BUCK_SW renamed /EC & MCU/BUCK_SW
- net /EC &amp; MCU/EC_SWD_VTREF renamed /EC & MCU/EC_SWD_VTREF
- net /EC &amp; MCU/HSE_IN renamed /EC & MCU/HSE_IN
- net /EC &amp; MCU/HSE_OUT renamed /EC & MCU/HSE_OUT
- net /EC &amp; MCU/HSE_XTAL_OUT renamed /EC & MCU/HSE_XTAL_OUT
- net /EC &amp; MCU/LSE_IN renamed /EC & MCU/LSE_IN
- net /EC &amp; MCU/LSE_OUT renamed /EC & MCU/LSE_OUT
- net /EC &amp; MCU/NRST_NET renamed /EC & MCU/NRST_NET
- net /EC &amp; MCU/SERVICE_MUX_RESET_REQ_N renamed /EC & MCU/SERVICE_MUX_RESET_REQ_N
- net /EC &amp; MCU/SOURCE_MGR_INT_N renamed /EC & MCU/SOURCE_MGR_INT_N
- net /EC &amp; MCU/SWCLK_NET renamed /EC & MCU/SWCLK_NET
- net /EC &amp; MCU/SWDIO_NET renamed /EC & MCU/SWDIO_NET
- net /EC &amp; MCU/VCAP1_NODE renamed /EC & MCU/VCAP1_NODE
- net /EC &amp; MCU/VCAP2_NODE renamed /EC & MCU/VCAP2_NODE
- net /Power &amp; Battery/AON_EFUSE_DVDT renamed /Power & Battery/AON_EFUSE_DVDT
- net /Power &amp; Battery/AON_EFUSE_ILM renamed /Power & Battery/AON_EFUSE_ILM
- net /Power &amp; Battery/AON_EFUSE_OV renamed /Power & Battery/AON_EFUSE_OV
- net /Power &amp; Battery/AON_EFUSE_UV renamed /Power & Battery/AON_EFUSE_UV
- net /Power &amp; Battery/AON_OR_RAW renamed /Power & Battery/AON_OR_RAW
- net /Power &amp; Battery/AUX_DC_DIV renamed /Power & Battery/AUX_DC_DIV
- net /Power &amp; Battery/AUX_DC_FUSED renamed /Power & Battery/AUX_DC_FUSED
- net /Power &amp; Battery/AUX_DC_PROTECTED renamed /Power & Battery/AUX_DC_PROTECTED
- net /Power &amp; Battery/AUX_EFUSE_BGATE renamed /Power & Battery/AUX_EFUSE_BGATE
- net /Power &amp; Battery/AUX_EFUSE_DRV renamed /Power & Battery/AUX_EFUSE_DRV
- net /Power &amp; Battery/AUX_EFUSE_DVDT renamed /Power & Battery/AUX_EFUSE_DVDT
- net /Power &amp; Battery/AUX_EFUSE_ILIM renamed /Power & Battery/AUX_EFUSE_ILIM
- net /Power &amp; Battery/AUX_EFUSE_IN_SYS renamed /Power & Battery/AUX_EFUSE_IN_SYS
- net /Power &amp; Battery/AUX_EFUSE_OV renamed /Power & Battery/AUX_EFUSE_OV
- net /Power &amp; Battery/AUX_EFUSE_Q2_GATE renamed /Power & Battery/AUX_EFUSE_Q2_GATE
- net /Power &amp; Battery/AUX_EFUSE_UV renamed /Power & Battery/AUX_EFUSE_UV
- net /Power &amp; Battery/AUX_PGTH renamed /Power & Battery/AUX_PGTH
- net /Power &amp; Battery/BATP_SENSE renamed /Power & Battery/BATP_SENSE
- net /Power &amp; Battery/BAT_CHARGER renamed /Power & Battery/BAT_CHARGER
- net /Power &amp; Battery/BTST1_NODE renamed /Power & Battery/BTST1_NODE
- net /Power &amp; Battery/BTST2_NODE renamed /Power & Battery/BTST2_NODE
- net /Power &amp; Battery/CHG_CE_HW_N renamed /Power & Battery/CHG_CE_HW_N
- net /Power &amp; Battery/CHG_TS_FIXED renamed /Power & Battery/CHG_TS_FIXED
- net /Power &amp; Battery/FG_BAT_DIV renamed /Power & Battery/FG_BAT_DIV
- net /Power &amp; Battery/FG_BAT_SENSE renamed /Power & Battery/FG_BAT_SENSE
- net /Power &amp; Battery/FG_CE renamed /Power & Battery/FG_CE
- net /Power &amp; Battery/FG_P1_TIE renamed /Power & Battery/FG_P1_TIE
- net /Power &amp; Battery/FG_REG25 renamed /Power & Battery/FG_REG25
- net /Power &amp; Battery/FG_SRN renamed /Power & Battery/FG_SRN
- net /Power &amp; Battery/FG_SRP renamed /Power & Battery/FG_SRP
- net /Power &amp; Battery/FG_TS renamed /Power & Battery/FG_TS
- net /Power &amp; Battery/ILIM_SET renamed /Power & Battery/ILIM_SET
- net /Power &amp; Battery/MAIN_SEL_INTVCC renamed /Power & Battery/MAIN_SEL_INTVCC
- net /Power &amp; Battery/MAIN_SEL_TMR renamed /Power & Battery/MAIN_SEL_TMR
- net /Power &amp; Battery/PMIC_QON_PIN renamed /Power & Battery/PMIC_QON_PIN
- net /Power &amp; Battery/PMID renamed /Power & Battery/PMID
- net /Power &amp; Battery/PROG_SET renamed /Power & Battery/PROG_SET
- net /Power &amp; Battery/REGN renamed /Power & Battery/REGN
- net /Power &amp; Battery/SDRV_GATE renamed /Power & Battery/SDRV_GATE
- net /Power &amp; Battery/SEL_STAGE2 renamed /Power & Battery/SEL_STAGE2
- net /Power &amp; Battery/ST2_AUX_FET_COMMON renamed /Power & Battery/ST2_AUX_FET_COMMON
- net /Power &amp; Battery/ST2_AUX_GATE renamed /Power & Battery/ST2_AUX_GATE
- net /Power &amp; Battery/ST2_AUX_OV renamed /Power & Battery/ST2_AUX_OV
- net /Power &amp; Battery/ST2_AUX_UV renamed /Power & Battery/ST2_AUX_UV
- net /Power &amp; Battery/ST2_MAIN_FET_COMMON renamed /Power & Battery/ST2_MAIN_FET_COMMON
- net /Power &amp; Battery/ST2_MAIN_GATE renamed /Power & Battery/ST2_MAIN_GATE
- net /Power &amp; Battery/ST2_MAIN_OV renamed /Power & Battery/ST2_MAIN_OV
- net /Power &amp; Battery/ST2_MAIN_UV renamed /Power & Battery/ST2_MAIN_UV
- net /Power &amp; Battery/ST2_SEL_INTVCC renamed /Power & Battery/ST2_SEL_INTVCC
- net /Power &amp; Battery/ST2_SEL_TMR renamed /Power & Battery/ST2_SEL_TMR
- net /Power &amp; Battery/ST2_USB_FET_COMMON renamed /Power & Battery/ST2_USB_FET_COMMON
- net /Power &amp; Battery/ST2_USB_GATE renamed /Power & Battery/ST2_USB_GATE
- net /Power &amp; Battery/ST2_USB_OV renamed /Power & Battery/ST2_USB_OV
- net /Power &amp; Battery/ST2_USB_UV renamed /Power & Battery/ST2_USB_UV
- net /Power &amp; Battery/STAT_DRV renamed /Power & Battery/STAT_DRV
- net /Power &amp; Battery/STAT_LED_A renamed /Power & Battery/STAT_LED_A
- net /Power &amp; Battery/SW1 renamed /Power & Battery/SW1
- net /Power &amp; Battery/SW2 renamed /Power & Battery/SW2
- net /Power &amp; Battery/USB_MAIN_FET_COMMON renamed /Power & Battery/USB_MAIN_FET_COMMON
- net /Power &amp; Battery/USB_MAIN_GATE renamed /Power & Battery/USB_MAIN_GATE
- net /Power &amp; Battery/USB_MAIN_OV renamed /Power & Battery/USB_MAIN_OV
- net /Power &amp; Battery/USB_MAIN_UV renamed /Power & Battery/USB_MAIN_UV
- net /Power &amp; Battery/VBUS_COMBINED renamed /Power & Battery/VBUS_COMBINED
- net /Power &amp; Battery/VBUS_DAMP renamed /Power & Battery/VBUS_DAMP
- net /Wi-Fi/Bluetooth &amp; OLEDs/OLED_A_SCL renamed /Wi-Fi/Bluetooth & OLEDs/OLED_A_SCL
- net /Wi-Fi/Bluetooth &amp; OLEDs/OLED_A_SDA renamed /Wi-Fi/Bluetooth & OLEDs/OLED_A_SDA
- net /Wi-Fi/Bluetooth &amp; OLEDs/OLED_B_SCL renamed /Wi-Fi/Bluetooth & OLEDs/OLED_B_SCL
- net /Wi-Fi/Bluetooth &amp; OLEDs/OLED_B_SDA renamed /Wi-Fi/Bluetooth & OLEDs/OLED_B_SDA
- net /Wi-Fi/Bluetooth &amp; OLEDs/WIFI_3V3 renamed /Wi-Fi/Bluetooth & OLEDs/WIFI_3V3
- net /Wi-Fi/Bluetooth &amp; OLEDs/WIFI_PERST_N renamed /Wi-Fi/Bluetooth & OLEDs/WIFI_PERST_N
- net /Wi-Fi/Bluetooth &amp; OLEDs/WIFI_REFCLK_E_N renamed /Wi-Fi/Bluetooth & OLEDs/WIFI_REFCLK_E_N
- net /Wi-Fi/Bluetooth &amp; OLEDs/WIFI_REFCLK_E_P renamed /Wi-Fi/Bluetooth & OLEDs/WIFI_REFCLK_E_P
- net /Wi-Fi/Bluetooth &amp; OLEDs/WIFI_W_DISABLE1_N renamed /Wi-Fi/Bluetooth & OLEDs/WIFI_W_DISABLE1_N
- net /Wi-Fi/Bluetooth &amp; OLEDs/WIFI_W_DISABLE2_N renamed /Wi-Fi/Bluetooth & OLEDs/WIFI_W_DISABLE2_N
- J4 pad 6: (no net) -> unconnected-(J4-Pin_6-Pad6)
- J422 pad TN: (no net) -> unconnected-(J422-PadTN)
- J73 pad A9: unconnected-(J73-VBUS-PadA4) -> unconnected-(J73-VBUS-PadA4)_1
- J73 pad B4: unconnected-(J73-VBUS-PadA4) -> unconnected-(J73-VBUS-PadA4)_2
- J73 pad B9: unconnected-(J73-VBUS-PadA4) -> unconnected-(J73-VBUS-PadA4)_3
- J901 pad 32: (no net) -> unconnected-(J901-Pin_32-Pad32)
- J902 pad 6: (no net) -> unconnected-(J902-Pin_6-Pad6)
